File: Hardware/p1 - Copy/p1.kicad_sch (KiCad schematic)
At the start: 4 parts, among them J1 Conn_01x02, SW1 SW_Push

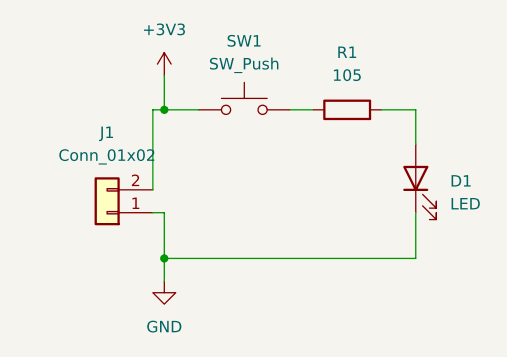
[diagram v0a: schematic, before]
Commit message: project finished with minor changes, pwr input is now a throughole component
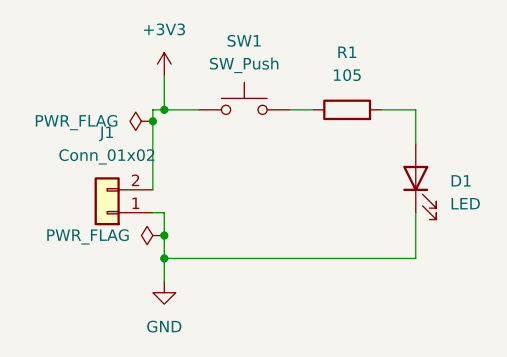
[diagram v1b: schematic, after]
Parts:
- D1: NOTES led change color -> led red
- SW1: MPN (none) -> 1825910-6
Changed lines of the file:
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@@
   (junction (at 58.42 68.58) (diameter 0) (color 0 0 0 0)
   )
+  (junction (at 57.15 69.85) (diameter 0) (color 0 0 0 0)
+  )
+  (junction (at 58.42 82.55) (diameter 0) (color 0 0 0 0)
+  )
   (junction (at 58.42 85.09) (diameter 0) (color 0 0 0 0)
   )
-  (wire (pts (xy 57.15 77.47) (xy 57.15 68.58))
+  (wire (pts (xy 57.15 69.85) (xy 57.15 68.58))
+    (stroke (width 0) (type default))
+  )
+  (wire (pts (xy 57.15 77.47) (xy 57.15 69.85))
     (stroke (width 0) (type default))
   )
@@
     (stroke (width 0) (type default))
   )
-  (wire (pts (xy 58.42 85.09) (xy 58.42 80.01))
+  (wire (pts (xy 58.42 85.09) (xy 58.42 82.55))
     (stroke (width 0) (type default))
   )
@@
     (stroke (width 0) (type default))
   )
+  (wire (pts (xy 58.42 82.55) (xy 58.42 80.01))
+    (stroke (width 0) (type default))
+  )
   (wire (pts (xy 82.55 68.58) (xy 86.36 68.58))
     (stroke (width 0) (type default))
+  )
+  (symbol (lib_id "power:PWR_FLAG") (at 57.15 69.85 90) (unit 1)
+    (in_bom yes) (on_board yes) (dnp no) (fields_autoplaced)
+    (property "Reference" "#FLG01" (at 55.245 69.85 0)
+      (effects (font (size 1.27 1.27)) hide)
+    )
+    (property "Value" "PWR_FLAG" (at 53.34 69.85 90)
+      (effects (font (size 1.27 1.27)) (justify left))
+    )
+    (property "Footprint" "" (at 57.15 69.85 0)
+      (effects (font (size 1.27 1.27)) hide)
+    )
+    (property "Datasheet" "~" (at 57.15 69.85 0)
+      (effects (font (size 1.27 1.27)) hide)
+    )
+    (pin "1")
+    (instances
+      (project "p1"
+        (path "/1e1b062d-fad0-427c-a622-c5b8a80b5268"
+          (reference "#FLG01") (unit 1)
+        )
+      )
+    )
   )
   (symbol (lib_id "device:LED") (at 86.36 76.2 90) (unit 1)
@@
       (effects (font (size 1.27 1.27)) hide)
     )
-    (property "NOTES" "led change color" (at 86.36 76.2 0)
+    (property "NOTES" "led red" (at 86.36 76.2 0)
       (effects (font (size 1.27 1.27)) hide)
     )
@@
     )
   )
+  (symbol (lib_id "power:PWR_FLAG") (at 58.42 82.55 90) (unit 1)
+    (in_bom yes) (on_board yes) (dnp no) (fields_autoplaced)
+    (property "Reference" "#FLG02" (at 56.515 82.55 0)
+      (effects (font (size 1.27 1.27)) hide)
+    )
+    (property "Value" "PWR_FLAG" (at 54.61 82.55 90)
+      (effects (font (size 1.27 1.27)) (justify left))
+    )
+    (property "Footprint" "" (at 58.42 82.55 0)
+      (effects (font (size 1.27 1.27)) hide)
+    )
+    (property "Datasheet" "~" (at 58.42 82.55 0)
+      (effects (font (size 1.27 1.27)) hide)
+    )
+    (pin "1")
+    (instances
+      (project "p1"
+        (path "/1e1b062d-fad0-427c-a622-c5b8a80b5268"
+          (reference "#FLG02") (unit 1)
+        )
+      )
+    )
+  )
   (symbol (lib_id "power:+3V3") (at 58.42 64.77 0) (unit 1)
     (in_bom yes) (on_board yes) (dnp no) (fields_autoplaced)
@@
       (effects (font (size 1.27 1.27)) hide)
     )
-    (property "Datasheet" "https://www.te.com/usa-en/product-1825910-6.datasheet.pdf" (at 78.74 68.58 0)
+    (property "Datasheet" "" (at 78.74 68.58 0)
       (effects (font (size 1.27 1.27)) hide)
     )
@@
       (effects (font (size 1.27 1.27)) hide)
     )
-    (property "Datasheet" "~" (at 67.31 63.5 0)
-      (effects (font (size 1.27 1.27)) hide)
-    )
-    (property "MPN" "" (at 67.31 68.58 0)
-      (effects (font (size 1.27 1.27)) hide)
-    )
+    (property "Datasheet" "https://www.te.com/usa-en/product-1825910-6.datasheet.pdf" (at 67.31 63.5 0)
+      (effects (font (size 1.27 1.27)) hide)
+    )
+    (property "MPN" "1825910-6" (at 67.31 68.58 0)
+      (effects (font (size 1.27 1.27)) hide)
+    )
